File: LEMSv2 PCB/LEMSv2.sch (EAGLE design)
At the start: 89 parts, among them J1 FEMALE 2x3, Q1 200mA/50V, Q10 200mA/50V, Q2 200mA/50V, Q3 MMBT3904, Q4 MMBT3904, Q5 200mA/50V, Q6 MMBT3904, Q7 200mA/50V, Q8 MMBT3904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

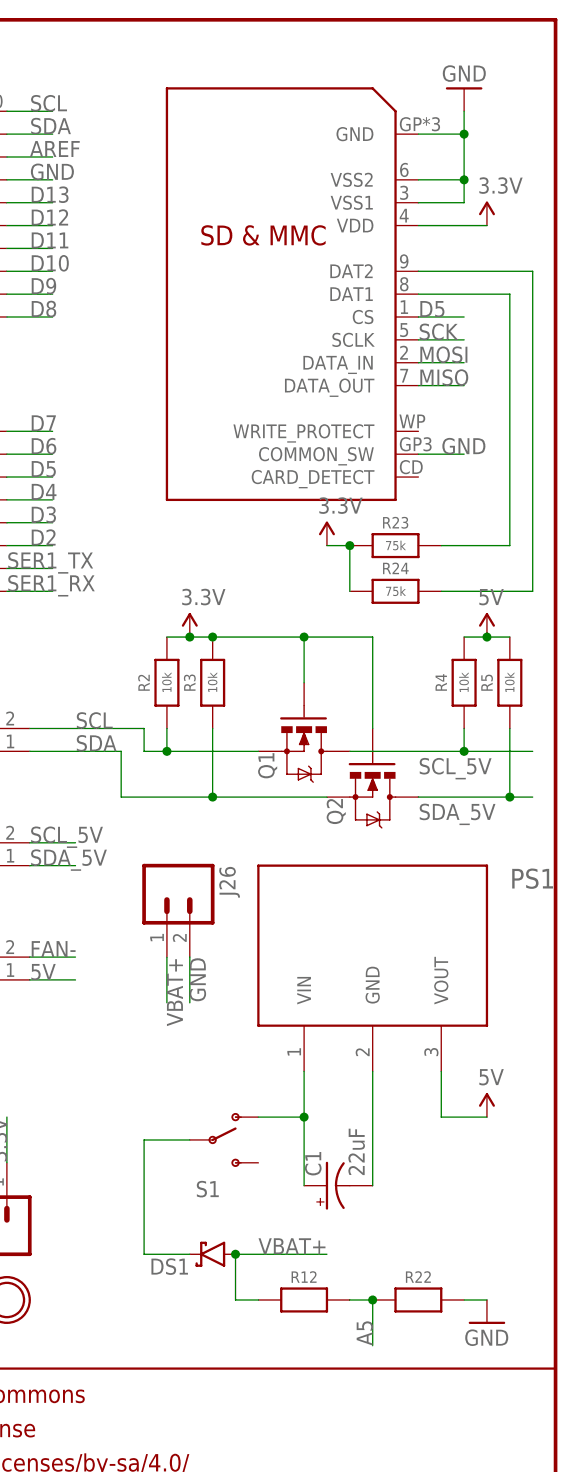
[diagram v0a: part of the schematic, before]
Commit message: Added gerbers and centroid files
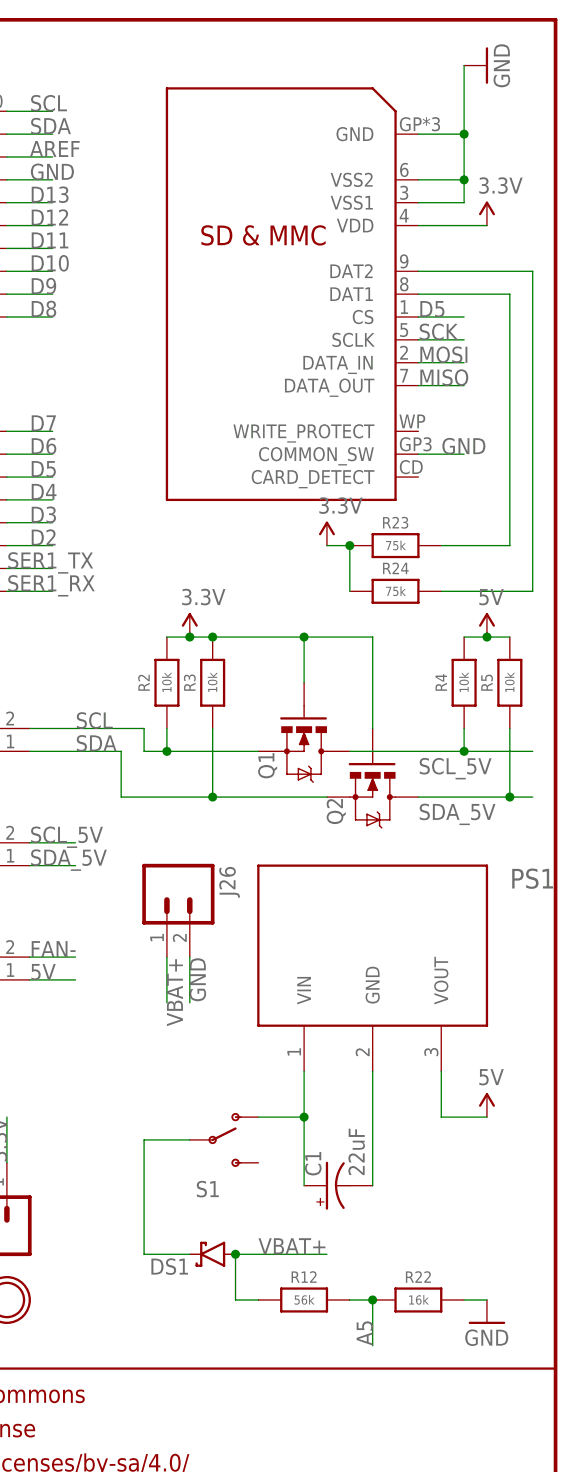
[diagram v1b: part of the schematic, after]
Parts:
- R12: value (none) -> 56k
- R22: value (none) -> 16k
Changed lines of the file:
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@@
 <part name="GND15" library="LEMSv2" deviceset="GND" device=""/>
 <part name="SUPPLY19" library="LEMSv2" deviceset="5V" device=""/>
-<part name="R12" library="LEMSv2" deviceset="RESISTOR" device="_0805"/>
-<part name="R22" library="LEMSv2" deviceset="RESISTOR" device="_0805"/>
+<part name="R12" library="LEMSv2" deviceset="RESISTOR" device="_0805" value="56k"/>
+<part name="R22" library="LEMSv2" deviceset="RESISTOR" device="_0805" value="16k"/>
 <part name="GND16" library="LEMSv2" deviceset="GND" device=""/>
 <part name="R23" library="LEMSv2" deviceset="RESISTOR" device="_0805" value="75k"/>
@@
 <instance part="FRAME1" gate="V" x="147.32" y="0"/>
 <instance part="U1" gate="G$1" x="220.98" y="154.94" rot="R180"/>
-<instance part="GND2" gate="1" x="238.76" y="177.8" rot="R180"/>
+<instance part="GND2" gate="1" x="241.3" y="180.34" rot="R90"/>
 <instance part="SUPPLY1" gate="G$1" x="241.3" y="162.56"/>
 <instance part="BT1" gate="G$1" x="101.6" y="175.26"/>
@@
 <pinref part="U1" gate="G$1" pin="VSS2"/>
 <wire x1="238.76" y1="167.64" x2="238.76" y2="172.72" width="0.1524" layer="91"/>
-<wire x1="238.76" y1="172.72" x2="238.76" y2="175.26" width="0.1524" layer="91"/>
+<wire x1="238.76" y1="172.72" x2="238.76" y2="180.34" width="0.1524" layer="91"/>
 <wire x1="233.68" y1="167.64" x2="238.76" y2="167.64" width="0.1524" layer="91"/>
 <junction x="238.76" y="167.64"/>
